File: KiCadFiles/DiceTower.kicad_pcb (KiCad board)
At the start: 2 copper layers, 132.5 x 132.5 mm, 27 parts, among them J1 USB_C_Receptacle_PowerOnly_6P, J2 Conn_01x05_Socket, J3 Conn_01x02_Pin, SW0 ChMxBl, SW1 ChMxBl, SW2 ChMxBl, SW3 ChMxBl, SW4 ChMxBl, SW5 ChMxBl, SW6 ChMxBl, U1 NHD-0420H1Z, U3 TPS73131DBV

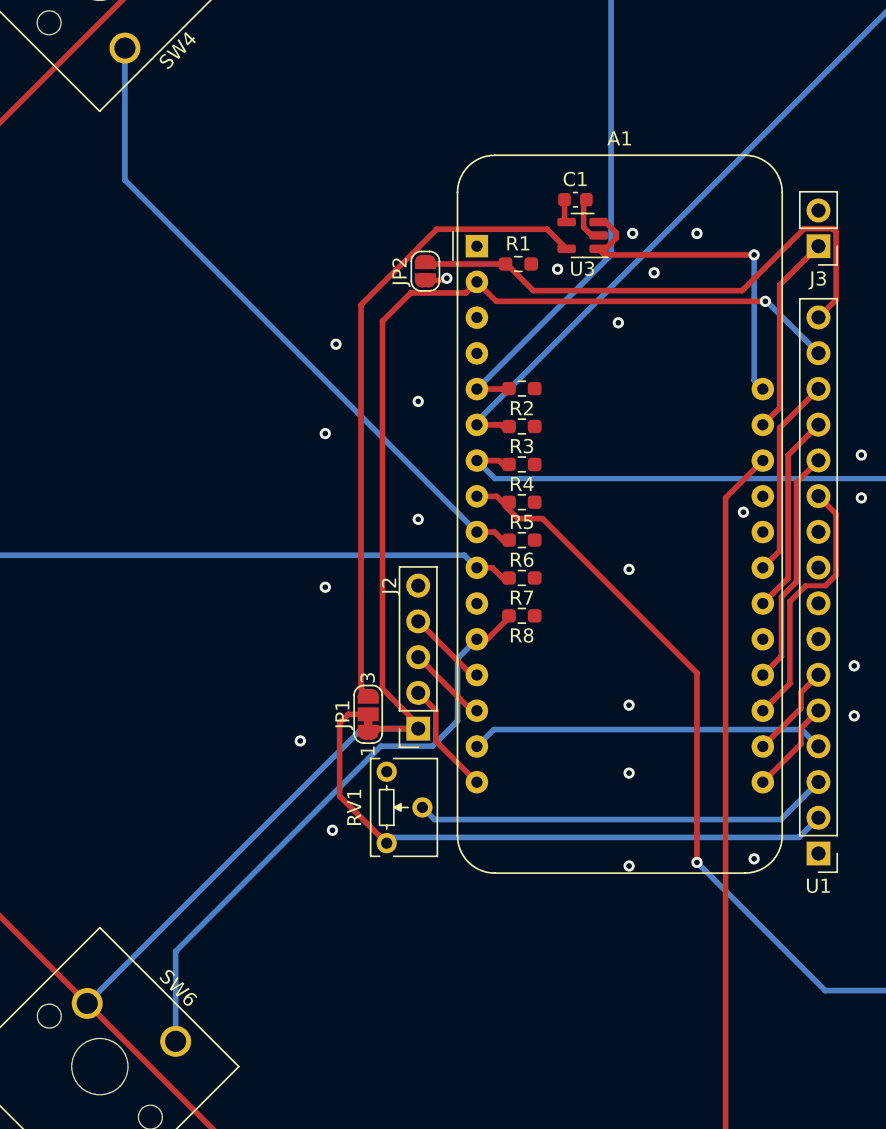
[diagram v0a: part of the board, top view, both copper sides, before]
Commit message: Change resistor location
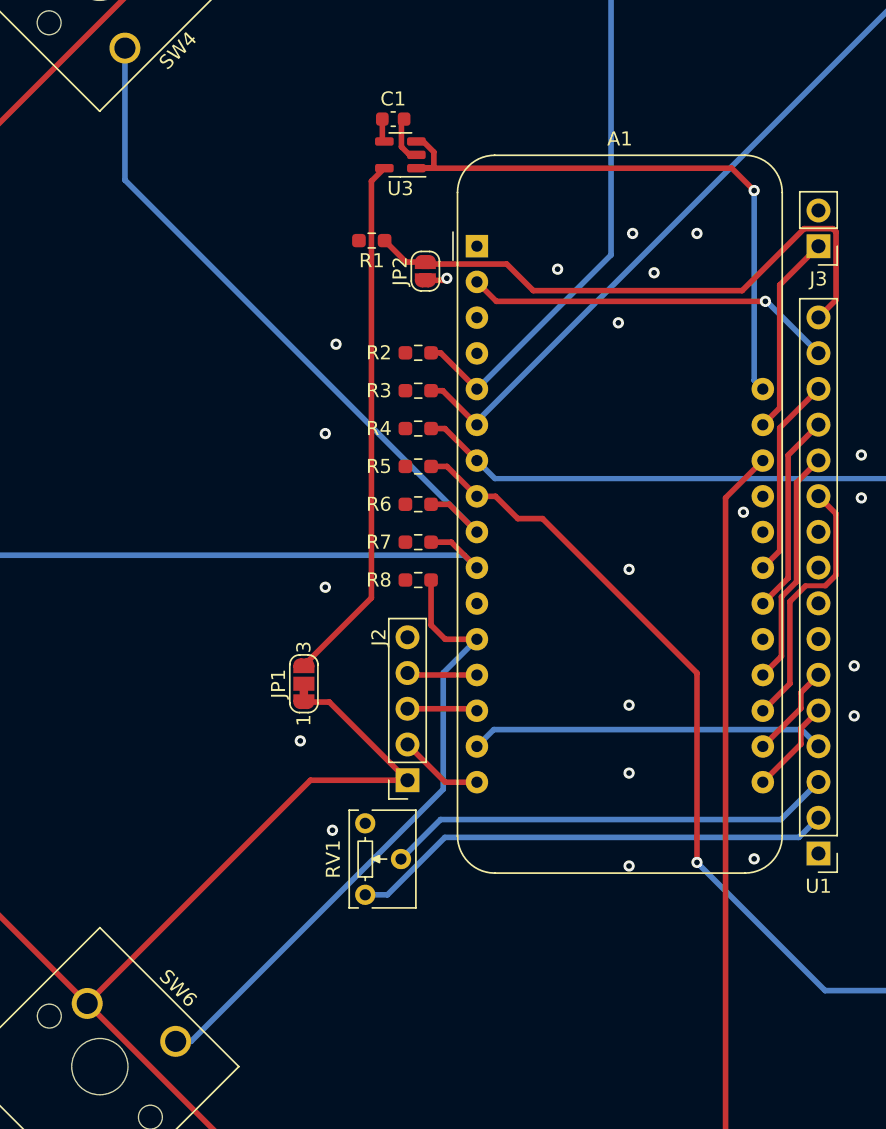
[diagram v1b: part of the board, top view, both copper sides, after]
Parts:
- moved U3 14.2 mm to (-17.5, -25.9)
- moved C1 14.2 mm to (-18.0, -28.4)
- moved R1 10.5 mm to (-19.6, -19.8), turned to 180 degrees
- moved R2 7.79 mm to (-16.3, -11.8), turned to 0 degrees
- moved R3 7.79 mm to (-16.3, -9.14), turned to 0 degrees
- moved R4 7.79 mm to (-16.3, -6.45), turned to 0 degrees
- moved R5 7.79 mm to (-16.3, -3.76), turned to 0 degrees
- moved R6 7.79 mm to (-16.3, -1.07), turned to 0 degrees
- moved R7 7.79 mm to (-16.3, 1.62), turned to 0 degrees
- moved R8 7.79 mm to (-16.3, 4.31), turned to 0 degrees
- moved JP1 5.06 mm to (-24.4, 11.7)
- moved RV1 3.97 mm to (-20.0, 21.6)
- moved J2 3.75 mm to (-17.0, 18.5)
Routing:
- net +3.3V: track 454.7 -> 420.5 mm
- net Net-(A1-VBAT): track 24.5 -> 42.9 mm
- net Net-(JP1-C): track 43.7 -> 34.5 mm
- net Net-(JP1-B): track 45.4 -> 37.7 mm
- net /SW3: track 71.7 -> 75.8 mm
- net Net-(JP2-B): track 38.5 -> 42.1 mm
- net /SW6: track 42.3 -> 45.0 mm
- net Net-(U1-VO): track 29.6 -> 31.9 mm
- net /SW0: track 46.8 -> 48.9 mm
- net /KEY: track 8.08 -> 6.04 mm
- net /SW1: track 60.6 -> 62.6 mm
- net /SW2: track 65.6 -> 67.4 mm
- net /SW4: track 47.2 -> 48.8 mm
- net /SW5: track 40.7 -> 42.2 mm
- net /S2: track 5.75 -> 4.99 mm
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
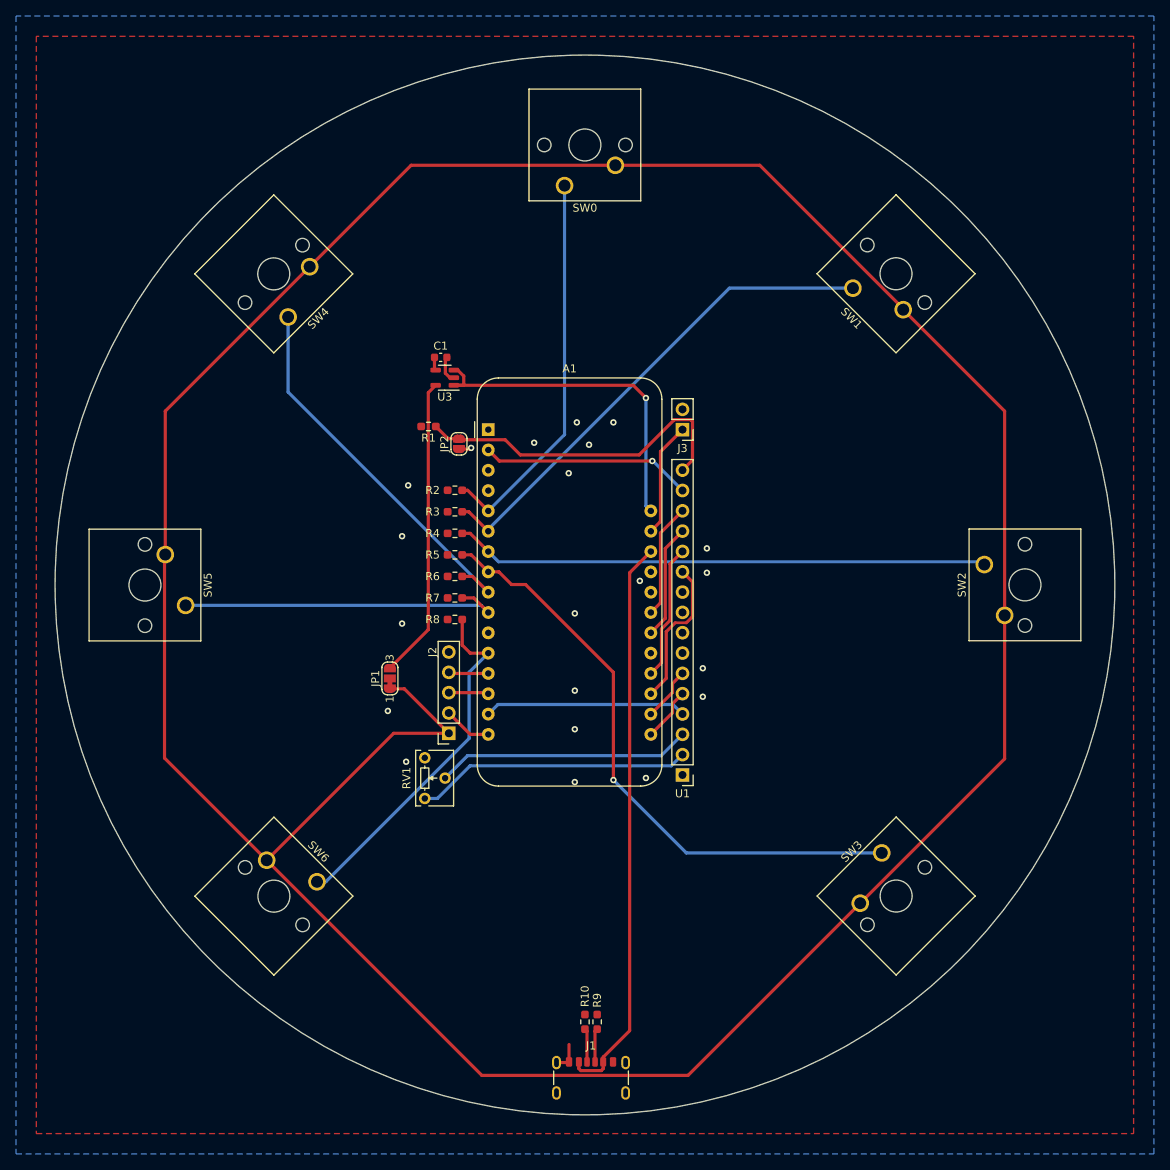
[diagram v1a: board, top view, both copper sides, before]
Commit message: Add mounting holes
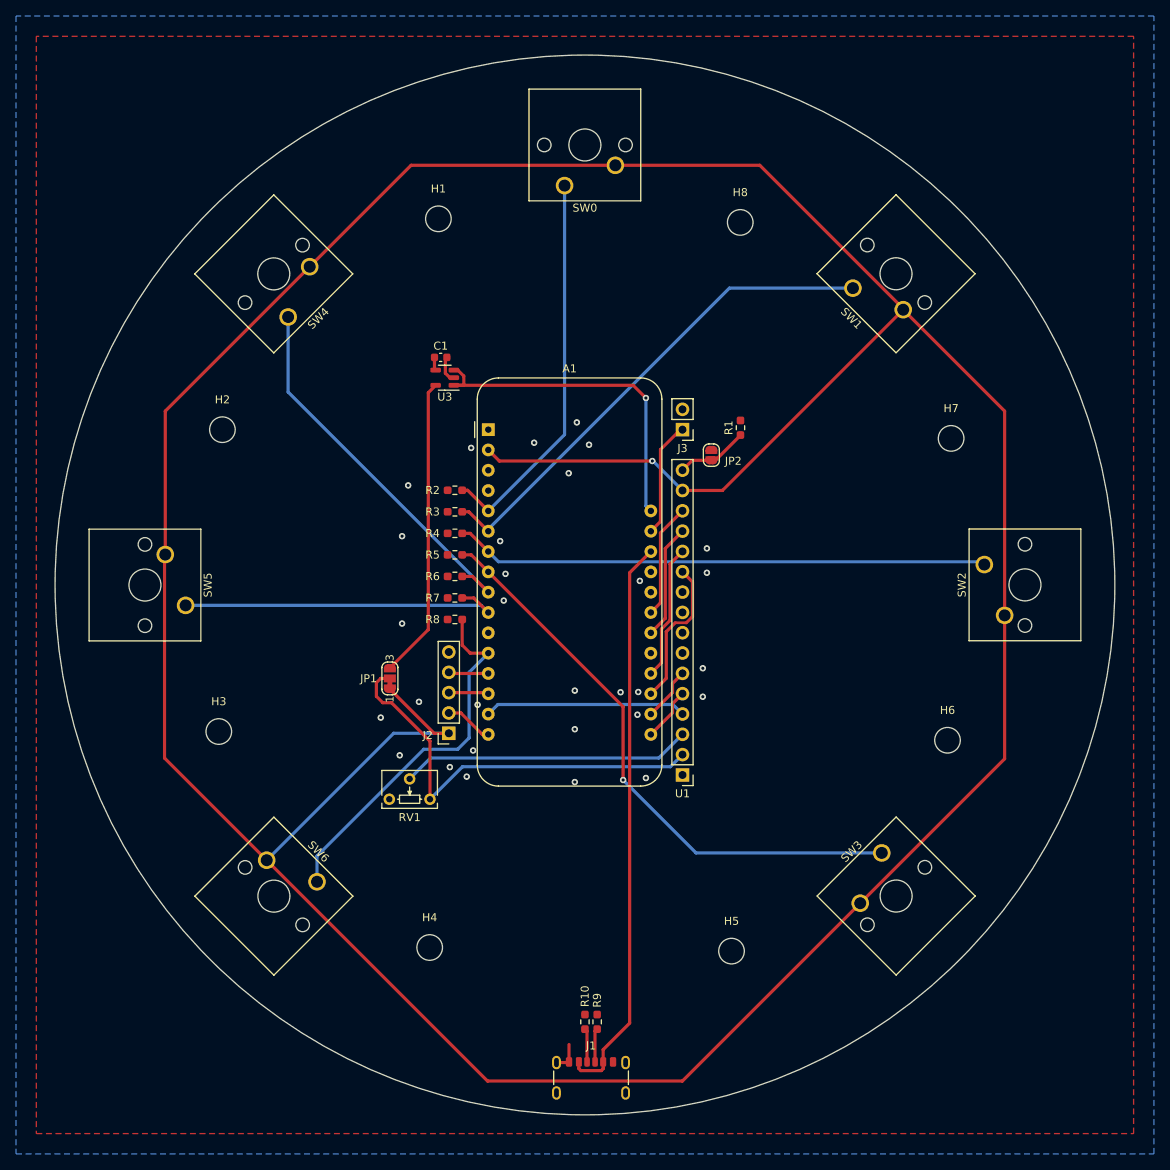
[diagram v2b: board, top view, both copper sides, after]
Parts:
- added H1: MountingHole, MountingHole:MountingHole_3.2mm_M3_ISO14580, F.Cu at (-18.3, -45.8)
- added H2: MountingHole, MountingHole:MountingHole_3.2mm_M3_ISO14580, F.Cu at (-45.3, -19.4)
- added H3: MountingHole, MountingHole:MountingHole_3.2mm_M3_ISO14580, F.Cu at (-45.8, 18.3)
- added H4: MountingHole, MountingHole:MountingHole_3.2mm_M3_ISO14580, F.Cu at (-19.4, 45.3)
- added H5: MountingHole, MountingHole:MountingHole_3.2mm_M3_ISO14580, F.Cu at (18.3, 45.8)
- added H6: MountingHole, MountingHole:MountingHole_3.2mm_M3_ISO14580, F.Cu at (45.3, 19.4)
- added H7: MountingHole, MountingHole:MountingHole_3.2mm_M3_ISO14580, F.Cu at (45.8, -18.3)
- added H8: MountingHole, MountingHole:MountingHole_3.2mm_M3_ISO14580, F.Cu at (19.4, -45.3)
- J2: value Conn_01x05_Socket -> Rot_Enc
- J3: value Conn_01x02_Pin -> MCU_EN
- JP2: value SolderJumper_2_Open -> Rser_LED
- moved R1 39.0 mm to (19.4, -19.7), turned to 90 degrees
- moved JP2 31.6 mm to (15.8, -16.2), turned to -90 degrees
- moved RV1 6.82 mm to (-24.5, 26.8), turned to 180 degrees
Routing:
- net +3.3V: track 420.5 -> 458.1 mm
- net Net-(JP2-B): track 42.1 -> 9.09 mm
- net Net-(JP1-C): track 34.5 -> 53.8 mm
- net Net-(U1-VO): track 31.9 -> 36.4 mm
- net /SW3: track 75.8 -> 73.2 mm
- net /SW6: track 45.0 -> 46.8 mm
- net GND: track 8.71 -> 7.32 mm, vias 21 -> 30

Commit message: Edit outline edgecuts
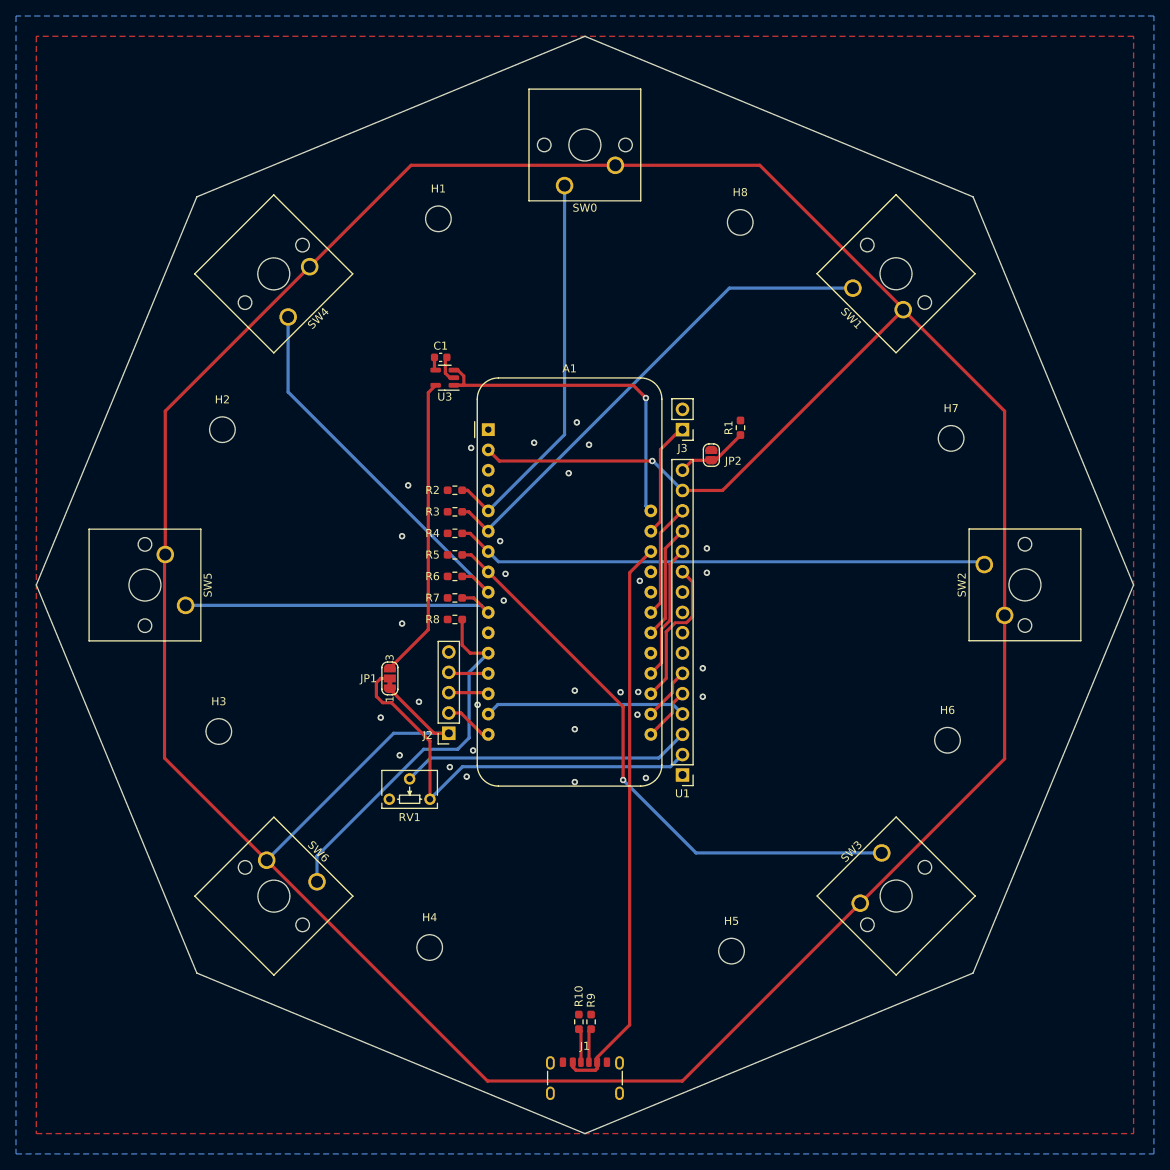
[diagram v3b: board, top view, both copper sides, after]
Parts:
- moved R10 0.76 mm to (-0.76, 54.6)
- moved R9 0.76 mm to (0.76, 54.6)
- moved J1 0.76 mm to (0.00, 62.7)
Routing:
- net GND: track 7.32 -> 3.55 mm
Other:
- board size 132.5 x 132.5 mm -> 137.2 x 137.2 mm
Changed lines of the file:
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@@
   )
   (footprint "Resistor_SMD:R_0603_1608Metric_Pad0.98x0.95mm_HandSolder" (layer "F.Cu")
-    (at 1.524 54.61 90)
+    (at 0.762 54.61 90)
     (descr "Resistor SMD 0603 (1608 Metric), square (rectangular) end terminal, IPC_7351 nominal with elongated pad for handsoldering. (Body size source: IPC-SM-782 page 72, https://www.pcb-3d.com/wordpress/wp-content/uploads/ipc-sm-782a_amendment_1_and_2.pdf), generated with kicad-footprint-generator")
     (tags "resistor handsolder")
@@
   )
   (footprint "Connector_USB:USB_C_Receptacle_GCT_USB4125-xx-x-0190_6P_TopMnt_Horizontal" (layer "F.Cu")
-    (at 0.76 62.7)
+    (at 0 62.738)
     (descr "USB Type C Receptacle, GCT, power-only, 6P, top mounted, horizontal, 3A, 1.9mm stake: https://gct.co/files/drawings/usb4125.pdf")
     (tags "USB C Type-C receptacle power-only charging-only 6P 6C right angled")
@@
   )
   (footprint "Resistor_SMD:R_0603_1608Metric_Pad0.98x0.95mm_HandSolder" (layer "F.Cu")
-    (at 0 54.61 90)
+    (at -0.762 54.61 90)
     (descr "Resistor SMD 0603 (1608 Metric), square (rectangular) end terminal, IPC_7351 nominal with elongated pad for handsoldering. (Body size source: IPC-SM-782 page 72, https://www.pcb-3d.com/wordpress/wp-content/uploads/ipc-sm-782a_amendment_1_and_2.pdf), generated with kicad-footprint-generator")
     (tags "resistor handsolder")
@@
     )
   )
-  (gr_circle (center 0 0) (end 66.04 -5.08)
-    (stroke (width 0.1) (type default)) (fill none) (layer "Edge.Cuts"))
+  (gr_poly
+    (pts
+      (xy 0 -68.58)
+      (xy -48.514 -48.514)
+      (xy -68.58 0)
+      (xy -48.514 48.514)
+      (xy 0 68.58)
+      (xy 48.514 48.514)
+      (xy 68.58 0)
+      (xy 48.514 -48.514)
+    )
+    (stroke (width 0.1) (type solid)) (fill none) (layer "Edge.Cuts"))
   (segment (start 8.2355 3.442793) (end 9.4355 2.242793) (width 0.4) (layer "F.Cu") (net 3))
   (segment (start 9.4355 -6.500707) (end 12.192 -9.257207) (width 0.4) (layer "F.Cu") (net 3))
@@
   (segment (start 10.0355 4.182793) (end 8.2355 5.982793) (width 0.4) (layer "F.Cu") (net 6))
   (segment (start -16.878817 -25.908) (end -16.3885 -25.908) (width 0.4) (layer "F.Cu") (net 7))
-  (segment (start -1.99 59.62) (end -1.99 57.446) (width 0.4) (layer "F.Cu") (net 7))
   (segment (start -17.451 -28.256) (end -17.451 -26.480183) (width 0.4) (layer "F.Cu") (net 7))
-  (segment (start -2.07 59.7) (end -1.99 59.62) (width 0.4) (layer "F.Cu") (net 7))
   (segment (start -17.259 -28.448) (end -17.451 -28.256) (width 0.4) (layer "F.Cu") (net 7))
   (segment (start -14.366 -16.989207) (end -14.224 -17.131207) (width 0.4) (layer "F.Cu") (net 7))
   (segment (start -17.451 -26.480183) (end -16.878817 -25.908) (width 0.4) (layer "F.Cu") (net 7))
-  (segment (start -3.56 59.7) (end -2.07 59.7) (width 0.4) (layer "F.Cu") (net 7))
   (via (at 14.732 13.97) (size 0.8) (drill 0.4) (layers "F.Cu" "B.Cu") (free) (net 7))
   (via (at 15.24 -1.524) (size 0.8) (drill 0.4) (layers "F.Cu" "B.Cu") (free) (net 7))
@@
   (segment (start 13.421 -15.58) (end 12.192 -14.351) (width 0.4) (layer "F.Cu") (net 30))
   (segment (start 19.44 -18.704314) (end 19.44 -18.74) (width 0.4) (layer "F.Cu") (net 30))
-  (segment (start 2.28 60.458) (end 2.28 59.62) (width 0.4) (layer "F.Cu") (net 37))
-  (segment (start 5.588 54.762) (end 5.588 -1.529707) (width 0.4) (layer "F.Cu") (net 37))
-  (segment (start 2.032 60.706) (end 2.28 60.458) (width 0.4) (layer "F.Cu") (net 37))
   (segment (start 5.588 -1.529707) (end 8.2355 -4.177207) (width 0.4) (layer "F.Cu") (net 37))
-  (segment (start -0.76 59.62) (end -0.76 60.454) (width 0.4) (layer "F.Cu") (net 37))
-  (segment (start -0.76 60.454) (end -0.508 60.706) (width 0.4) (layer "F.Cu") (net 37))
-  (segment (start 2.28 59.62) (end 2.28 58.07) (width 0.4) (layer "F.Cu") (net 37))
-  (segment (start 2.28 58.07) (end 5.588 54.762) (width 0.4) (layer "F.Cu") (net 37))
-  (segment (start -0.508 60.706) (end 2.032 60.706) (width 0.4) (layer "F.Cu") (net 37))
-  (segment (start 0.26 59.62) (end 0.26 55.7825) (width 0.4) (layer "F.Cu") (net 38))
-  (segment (start 0.26 55.7825) (end 0 55.5225) (width 0.4) (layer "F.Cu") (net 38))
-  (segment (start 1.26 55.7865) (end 1.26 59.62) (width 0.4) (layer "F.Cu") (net 39))
-  (segment (start 1.524 55.5225) (end 1.26 55.7865) (width 0.4) (layer "F.Cu") (net 39))
+  (segment (start -1.52 60.258) (end -1.12 60.658) (width 0.4) (layer "F.Cu") (net 37))
+  (segment (start -1.12 60.658) (end 1.318 60.658) (width 0.4) (layer "F.Cu") (net 37))
+  (segment (start 1.52 59.658) (end 1.52 59.058) (width 0.4) (layer "F.Cu") (net 37))
+  (segment (start -1.52 59.658) (end -1.52 60.258) (width 0.4) (layer "F.Cu") (net 37))
+  (segment (start 1.318 60.658) (end 1.52 60.456) (width 0.4) (layer "F.Cu") (net 37))
+  (segment (start 5.588 54.99) (end 5.588 -1.529707) (width 0.4) (layer "F.Cu") (net 37))
+  (segment (start 1.52 59.058) (end 5.588 54.99) (width 0.4) (layer "F.Cu") (net 37))
+  (segment (start 1.52 60.456) (end 1.52 59.658) (width 0.4) (layer "F.Cu") (net 37))
+  (segment (start -0.5 55.7845) (end -0.5 59.658) (width 0.4) (layer "F.Cu") (net 38))
+  (segment (start -0.762 55.5225) (end -0.5 55.7845) (width 0.4) (layer "F.Cu") (net 38))
+  (segment (start 0.762 55.5225) (end 0.5 55.7845) (width 0.4) (layer "F.Cu") (net 39))
+  (segment (start 0.5 55.7845) (end 0.5 59.658) (width 0.4) (layer "F.Cu") (net 39))
   (zone (net 7) (net_name "GND") (layer "F.Cu") (hatch edge 0.5)
     (connect_pads (clearance 0.25))

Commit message: Collect all the chaos nachos!
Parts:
- added G***: LOGO, LOGO, B.Cu at (-2.03, -0.37)
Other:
- board text added: "JLCJLCJLCJLC"
- board text added: "The Fastest Mean Bean Machine Player Alive"
